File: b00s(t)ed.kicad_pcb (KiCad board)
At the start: 2 copper layers, 3 parts, among them P1 XT60PW, Q1 FDMC86012, Q2 FDMC86012

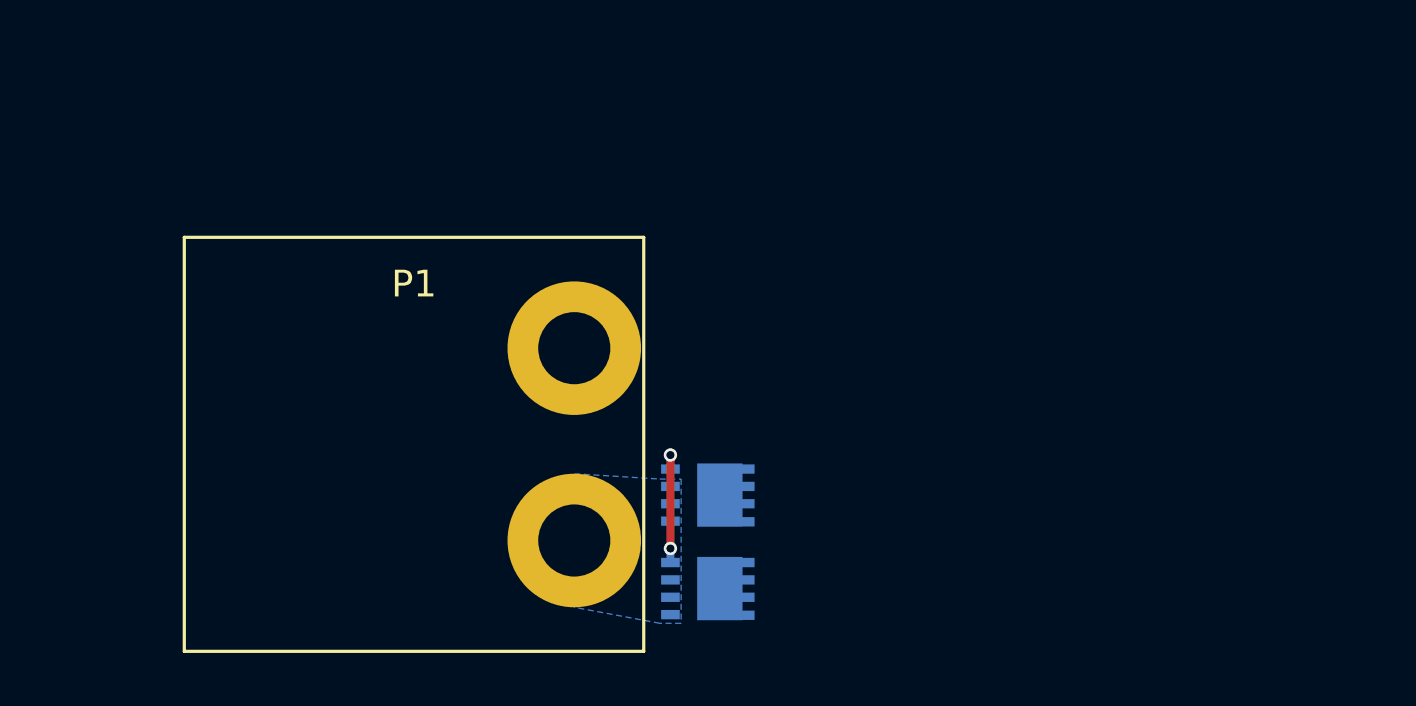
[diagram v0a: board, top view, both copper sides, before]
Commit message: Fixed connectors
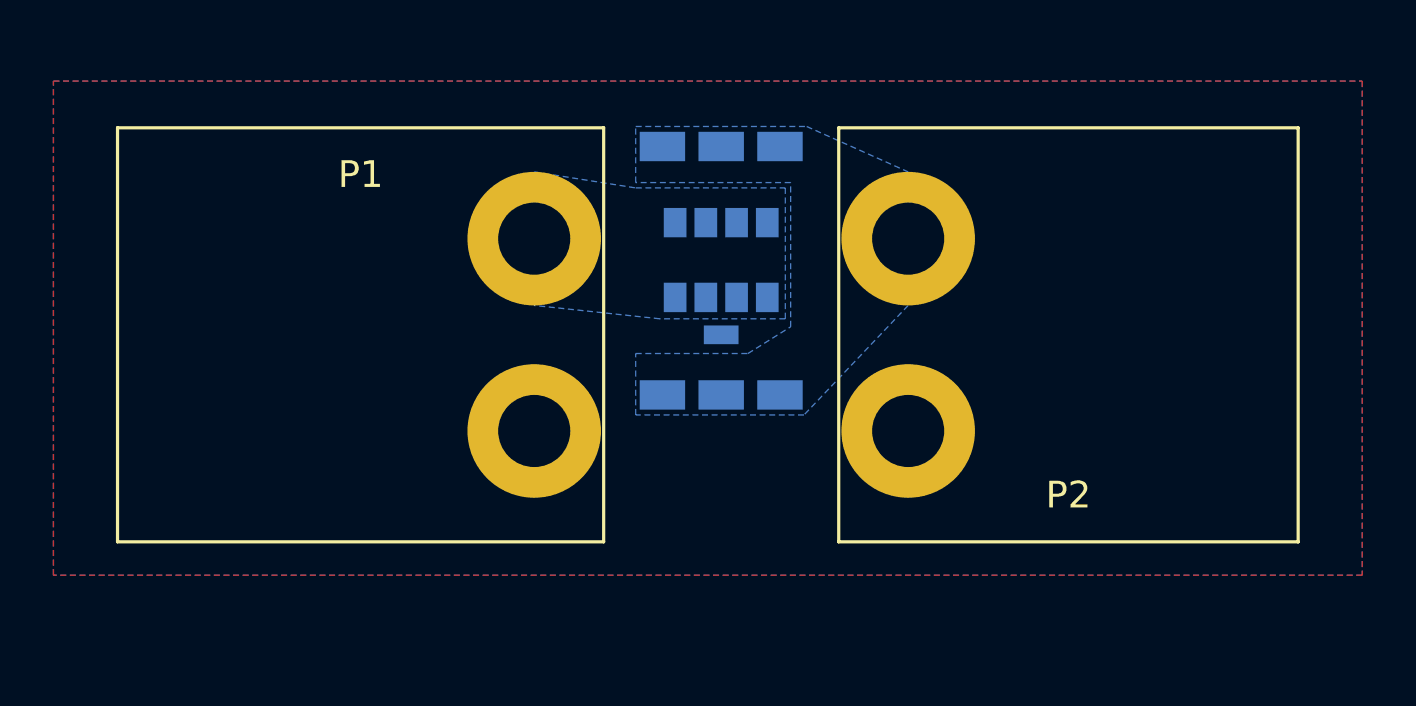
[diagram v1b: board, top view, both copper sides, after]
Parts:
- removed Q2: FDMC86012, Package_TO_SOT_SMD:Power33
- added P2: XT60PW, Connector:XT60PW-F, F.Cu at (154.5, 70.0)
- P1: footprint Connector:XT60PW-F -> Connector:XT60PW-M
- Q1: value FDMC86012 -> IRL7472L1; footprint Package_TO_SOT_SMD:Power33 -> Package_DirectFET:DirectFET_L8
- moved Q1 11.9 mm to (141.5, 67.6), turned to 90 degrees
- moved P1 4.56 mm to (128.0, 70.0)
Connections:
- P1 pad -: (no net) -> GND
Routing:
- net Net-(Q1-PadG): track 4.65 -> 0.00 mm, vias 2 -> 0
- added copper zone on B.Cu, net GND
- added copper zone on F.Cu, net GND
- added copper zone on B.Cu, net Net-(P2-Pad+)
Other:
- net class HV added: clearance 1, trace_width 0.15, via_dia 0.8, via_drill 0.4

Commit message: backup
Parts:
- removed P1: XT60PW, Connector:XT60PW-M
- removed P2: XT60PW, Connector:XT60PW-F
- added C1: C, Capacitor_SMD:C_1206_3216Metric, B.Cu at (133.6, 69.4)
- added C2: C, Capacitor_SMD:C_1206_3216Metric, B.Cu at (136.2, 69.4)
- added C3: C, Capacitor_SMD:C_1206_3216Metric, B.Cu at (140.0, 68.2)
- added C4: C, Capacitor_SMD:C_1206_3216Metric, B.Cu at (143.8, 69.4)
- added D1: D, Diode_SMD:D_SMB, F.Cu at (132.5, 71.0)
- added U1: LM74610-Q1, Package_SO:S-PDSO-G8, B.Cu at (140.0, 65.0)
- Q1: moved to F.Cu
- moved Q1 1.62 mm to (140.0, 67.0), turned to 270 degrees
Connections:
- Q1 pad 1: Net-(P2-Pad+) -> /OUT
- Q1 pad 2: (no net) -> Net-(Q1-Pad2)
- Q1 pad 3: Net-(P1-Pad+) -> +BATT
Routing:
- net -BATT: track 0.00 -> 8.20 mm, vias 0 -> 5
- net Net-(Q1-Pad2): track 0.00 -> 6.44 mm, vias 0 -> 1
- net Net-(C3-Pad2): track 0.00 -> 4.12 mm
- net Net-(C3-Pad1): track 0.00 -> 2.56 mm
- net +BATT: track 0.00 -> 1.80 mm, vias 0 -> 7
- added copper zone on B.Cu, net +BATT
- added copper zone on F.Cu, net +BATT
- added copper zone on B.Cu, net -BATT
- added copper zone on F.Cu, net -BATT
- added copper zone on B.Cu, net /OUT
- added copper zone on F.Cu, net /OUT
- removed copper zone on B.Cu, net GND
- removed copper zone on F.Cu, net GND
- removed copper zone on B.Cu, net Net-(P1-Pad+)
- removed copper zone on B.Cu, net Net-(P2-Pad+)
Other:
- board outline added: 21 x 20 mm
- net class Default: trace_width 0.15 -> 0.3
- net class HV removed

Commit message: First version ready for order
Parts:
- added C5: C, Capacitor_SMD:C_1206_3216Metric, B.Cu at (146.4, 69.4)
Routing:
- net -BATT: track 8.20 -> 12.5 mm
- net /OUT: track 0.00 -> 2.52 mm, vias 0 -> 7
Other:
- net class Default: via_dia 0.8 -> 0.7
- rule pad_to_mask_clearance: 0.051 -> 0
- rule solder_mask_min_width: 0.25 -> 0.2
- board text added: "2019-02-02"
- board text added: "b00s(t)ed"
- board text added: "by turbo function"

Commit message: ordered
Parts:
- added D2: VLMTG1400, Diode_SMD:D_0603_1608Metric, F.Cu at (147.0, 71.9)
- added Q2: 2N7002W, Package_TO_SOT_SMD:SOT-323_SC-70, B.Cu at (140.0, 70.6)
- added U2: NSI50010YT1G, Digikey:SOD-123, B.Cu at (143.6, 69.6)
- Q1: value IRL7472L1 -> IRF7739L1
- moved C4 2.21 mm to (146.0, 69.6)
- moved C5 2.01 mm to (148.4, 69.6)
- moved C1 0.36 mm to (133.3, 69.6)
- moved C2 0.36 mm to (135.9, 69.6)
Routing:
- net -BATT: track 12.5 -> 23.8 mm, vias 5 -> 1
- net Net-(Q1-Pad2): track 6.44 -> 13.5 mm
- net +BATT: track 1.80 -> 6.13 mm
- net Net-(Q2-Pad1): track 0.00 -> 3.88 mm
- net Net-(D2-Pad2): track 0.00 -> 3.01 mm, vias 0 -> 1
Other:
- board size 21 x 20 mm -> 21 x 19 mm
- net class HV added: clearance 0.3, trace_width 0.3, via_dia 0.7, via_drill 0.4
- net class Power added: clearance 0.15, trace_width 1.2, via_dia 0.7, via_drill 0.4
- rule pad_to_mask_clearance: 0 -> 0.03
- rule solder_mask_min_width: 0.2 -> 0.15
- board text added: "1-6s"
- board text added: "2019-02-04"
- board text added: "BOOST!"
- board text added: "TURBOfunction.com"
- board text removed: "2019-02-02"
- board text removed: "by turbo function"
